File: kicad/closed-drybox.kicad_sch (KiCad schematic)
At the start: 30 parts, among them J1 Power_Jack, M1 Fan, M2 Fan, Q1 AO3400A, Q2 AO3400A, Q3 AO3400A, Q4 AO3400A, Q5 AO3400A, Q6 AO3400A, Q7 AO3400A, SW1 SW_PWR, U1 XIAO-ESP32-C6, U3 AMS1117-3.3

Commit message: add PCB
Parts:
- removed F1: Fuse, symbol Device:Fuse
- removed JP2, JP3: SolderJumper_2_Open, Jumper:SolderJumper-2_P1.3mm_Open_RoundedPad1.0x1.5mm, symbol Jumper:SolderJumper_2_Open
- removed SW1: SW_PWR, Connector_PinHeader_2.54mm:PinHeader_1x02_P2.54mm_Vertical, symbol CustomLibary:SW_PWR
- added H1, H2, H3, H4: MountingHole_Pad, MountingHole:MountingHole_3.2mm_M3_DIN965_Pad, symbol Mechanical:MountingHole_Pad
- C1: footprint (none) -> Capacitor_SMD:C_1206_3216Metric
- C6: renamed from C2; footprint (none) -> Capacitor_SMD:C_1206_3216Metric
- Q1: renamed from Q2; footprint Package_TO_SOT_SMD:SOT-23_Handsoldering -> Package_TO_SOT_SMD:SOT-23
- Q2: renamed from Q3; footprint Package_TO_SOT_SMD:SOT-23_Handsoldering -> Package_TO_SOT_SMD:SOT-23
- Q3: renamed from Q1; footprint Package_TO_SOT_SMD:SOT-23_Handsoldering -> Package_TO_SOT_SMD:SOT-23
- Q4, Q5, Q6, Q7: footprint Package_TO_SOT_SMD:SOT-23_Handsoldering -> Package_TO_SOT_SMD:SOT-23
- renumbered C4 to C2, C5 to C3, C6 to C4, C7 to C5, D3 to D1, D4 to D2, M2 to M1, M1 to M2, U3 to U1, U1 to U2
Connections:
- net GND: now also H1.1, H2.1, H3.1, H4.1
- net power measurement/IN: now also J1.1

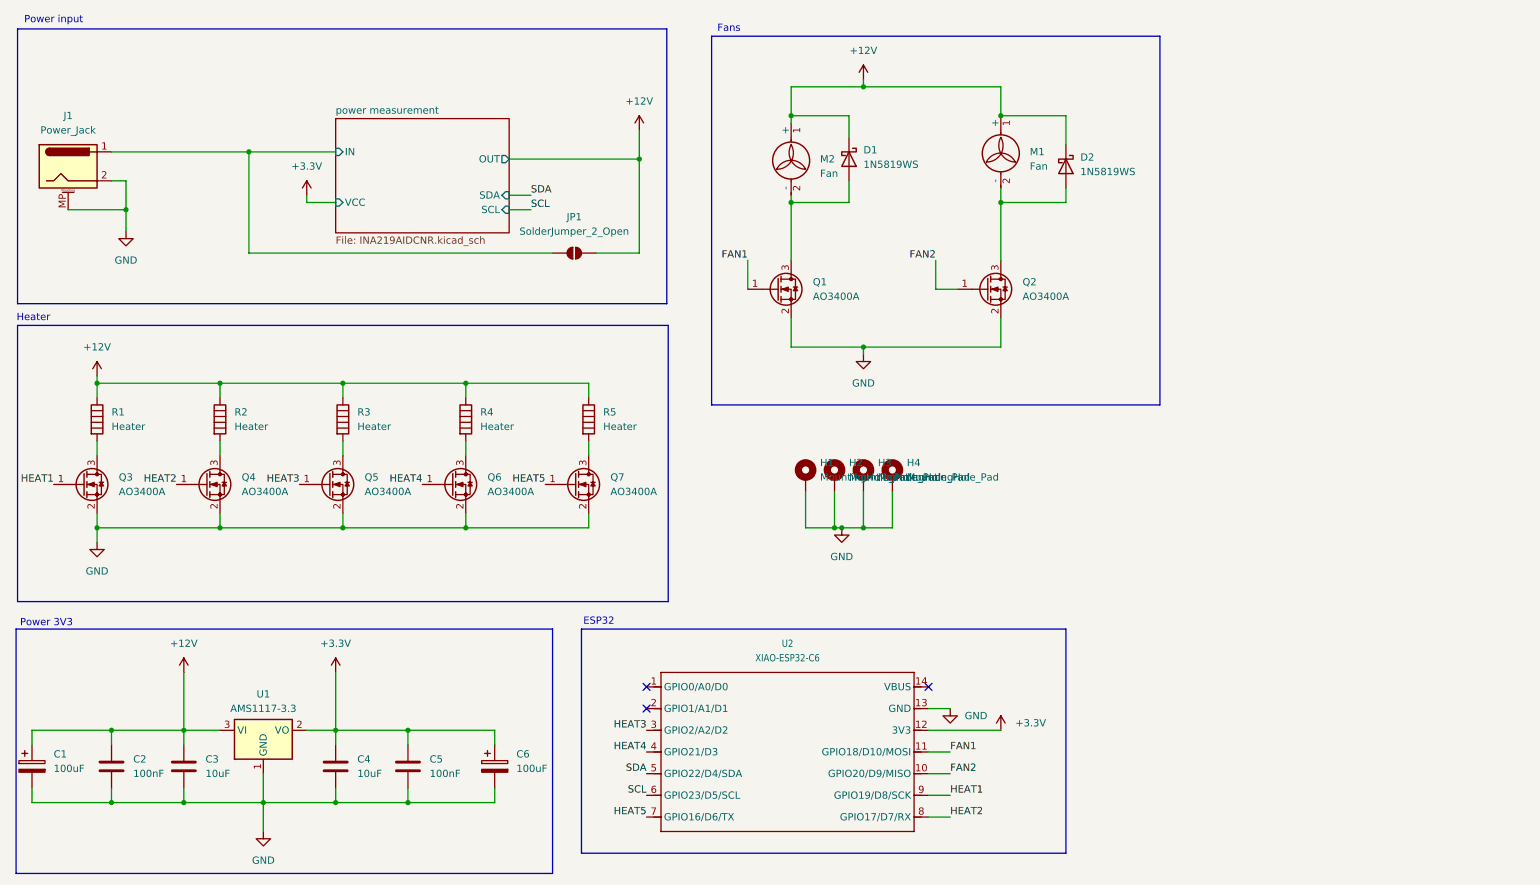
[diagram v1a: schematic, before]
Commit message: update schematic
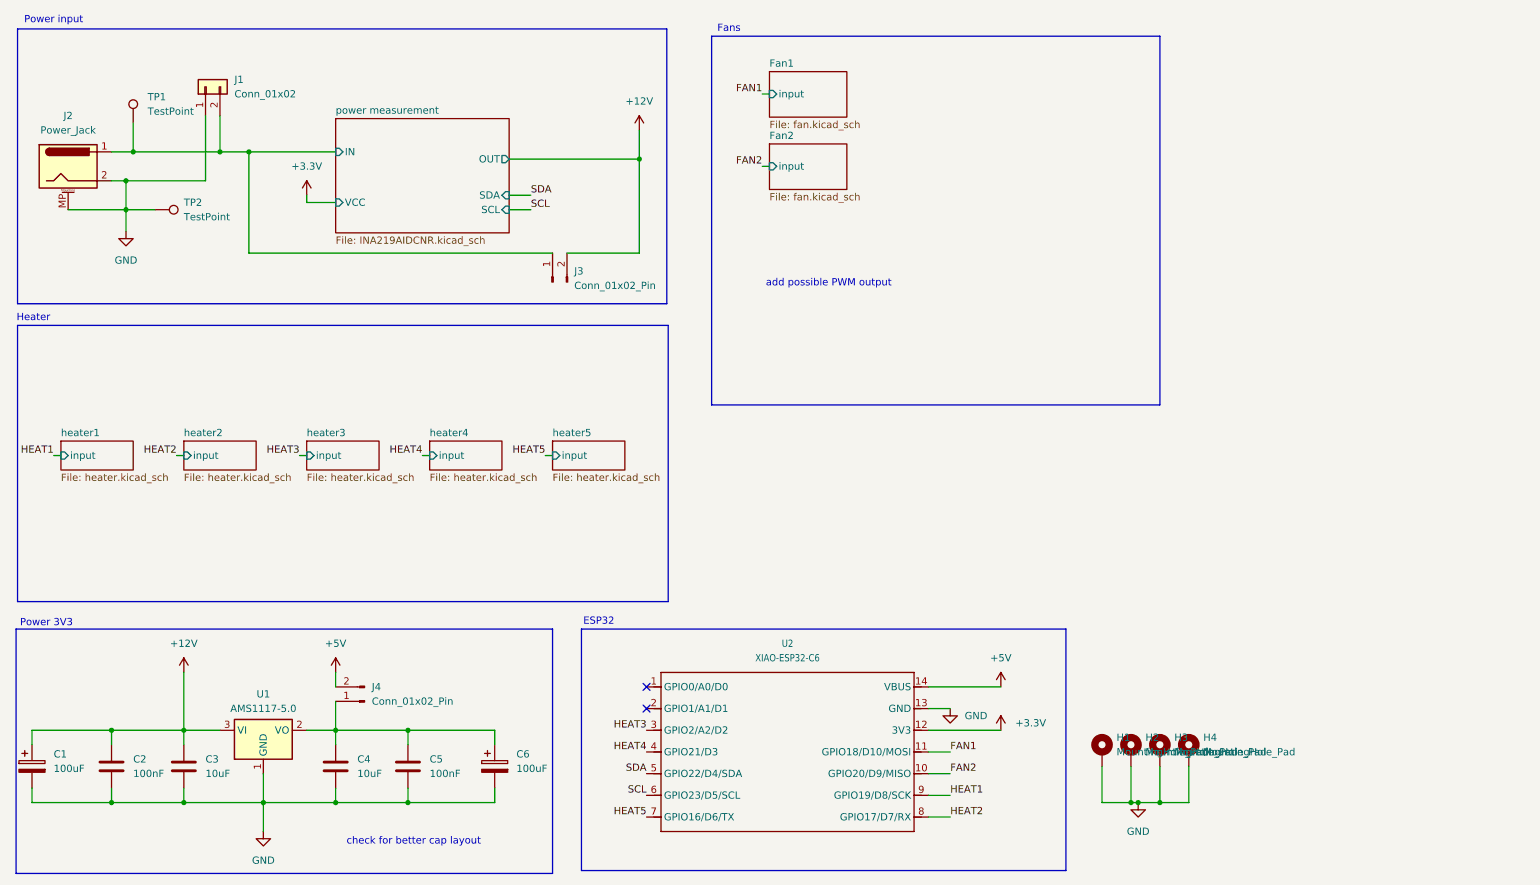
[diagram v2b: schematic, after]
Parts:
- removed D1, D2: 1N5819WS, Diode_SMD:D_SOD-323, symbol Diode:1N5819WS
- removed JP1: SolderJumper_2_Open, Jumper:SolderJumper-2_P1.3mm_Open_RoundedPad1.0x1.5mm, symbol Jumper:SolderJumper_2_Open
- removed M1, M2: Fan, Connector_JST:JST_XH_S2B-XH-A_1x02_P2.50mm_Horizontal, symbol Motor:Fan
- removed Q1, Q2, Q3, Q4, Q5, Q6, Q7: AO3400A, Package_TO_SOT_SMD:SOT-23, symbol Transistor_FET:AO3400A
- removed R1, R2, R3, R4, R5: Heater, Connector_JST:JST_XH_S2B-XH-A_1x02_P2.50mm_Horizontal, symbol Device:Heater
- removed U1: AMS1117-3.3, Package_TO_SOT_SMD:SOT-223-3_TabPin2, symbol Regulator_Linear:AMS1117-3.3
- added J1: Conn_01x02, Connector_JST:JST_XH_S2B-XH-A-1_1x02_P2.50mm_Horizontal, symbol Connector_Generic:Conn_01x02
- added J3, J4: Conn_01x02_Pin, Connector_PinHeader_2.54mm:PinHeader_1x02_P2.54mm_Vertical, symbol Connector:Conn_01x02_Pin
- added TP1, TP2: TestPoint, TestPoint:TestPoint_Pad_D2.5mm, symbol Connector:TestPoint
- added U1: AMS1117-5.0, Package_TO_SOT_SMD:SOT-223-3_TabPin2, symbol Regulator_Linear:AMS1117-5.0
- renumbered J1 to J2
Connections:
- net +12V: now also J3.2 (Pin_2), U1.3 (VI)
- net +3.3V: no longer C4.1, C5.1, C6.1
- net GND: now also J1.1 (Pin_1), TP2.1, U1.1 (GND)
- net power measurement/IN: now also J1.2 (Pin_2), J3.1 (Pin_1), TP1.1
- net +5V: now reaches U2.14 (VBUS)
- net +5V: now also J4.2 (Pin_2)
- new net: C4.1, C5.1, C6.1, J4.1 (Pin_1), U1.2 (VO)
- no-connect marks 3 -> 2
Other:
- added sheet Fan1 (fan.kicad_sch)
- added sheet Fan2 (fan.kicad_sch)
- added sheet heater1 (heater.kicad_sch)
- added sheet heater2 (heater.kicad_sch)
- added sheet heater3 (heater.kicad_sch)
- added sheet heater4 (heater.kicad_sch)
- added sheet heater5 (heater.kicad_sch)
- note added: "add possible PWM output"
- note added: "check for better cap layout"
- moved on the sheet: H1, H2, H3, H4

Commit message: added connectors
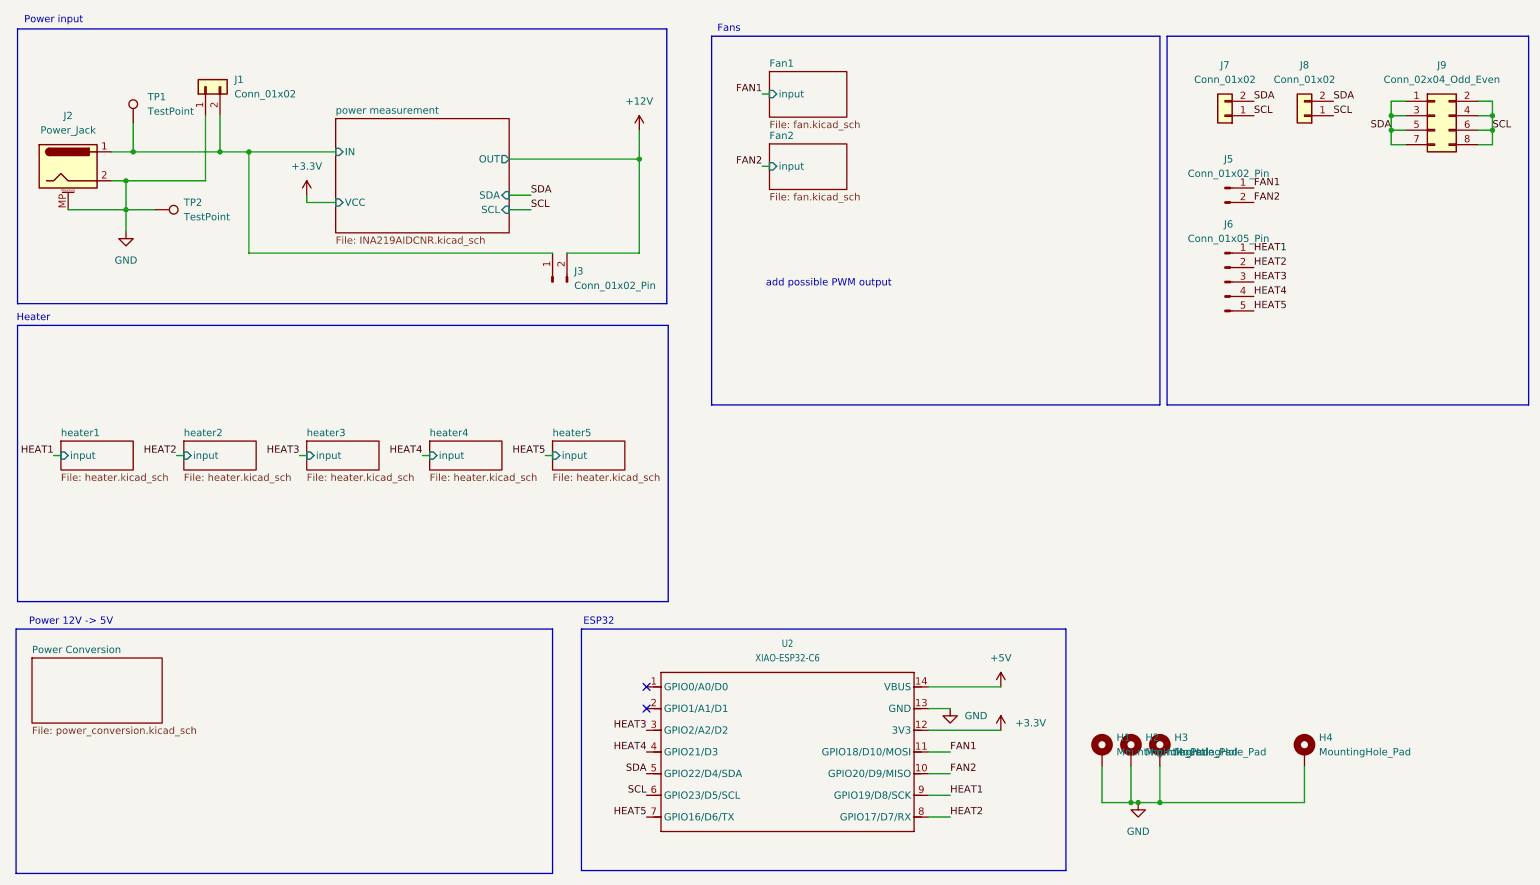
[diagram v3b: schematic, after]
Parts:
- removed C1, C6: 100uF, Capacitor_SMD:C_1206_3216Metric, symbol Device:C_Polarized
- removed C2, C5: 100nF, Capacitor_SMD:C_0603_1608Metric, symbol Device:C
- removed C3, C4: 10uF, Capacitor_SMD:C_0603_1608Metric, symbol Device:C
- removed J4: Conn_01x02_Pin, Connector_PinHeader_2.54mm:PinHeader_1x02_P2.54mm_Vertical, symbol Connector:Conn_01x02_Pin
- removed U1: AMS1117-5.0, Package_TO_SOT_SMD:SOT-223-3_TabPin2, symbol Regulator_Linear:AMS1117-5.0
- added J5: Conn_01x02_Pin, Connector_PinHeader_2.54mm:PinHeader_1x02_P2.54mm_Vertical, symbol Connector:Conn_01x02_Pin
- added J6: Conn_01x05_Pin, Connector_PinHeader_2.54mm:PinHeader_1x05_P2.54mm_Vertical, symbol Connector:Conn_01x05_Pin
- added J7, J8: Conn_01x02, Connector_JST:JST_XH_S2B-XH-A-1_1x02_P2.50mm_Horizontal, symbol Connector_Generic:Conn_01x02
- added J9: Conn_02x04_Odd_Even, symbol Connector_Generic:Conn_02x04_Odd_Even
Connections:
- net FAN1: now also J5.1 (Pin_1)
- net FAN2: now also J5.2 (Pin_2)
- net HEAT1: now also J6.1 (Pin_1)
- net HEAT2: now also J6.2 (Pin_2)
- net HEAT3: now also J6.3 (Pin_3)
- net HEAT4: now also J6.4 (Pin_4)
- net HEAT5: now also J6.5 (Pin_5)
- net SCL: now also J7.1 (Pin_1), J8.1 (Pin_1), J9.2 (Pin_2), J9.4 (Pin_4), J9.6 (Pin_6), J9.8 (Pin_8)
- net SDA: now also J7.2 (Pin_2), J8.2 (Pin_2), J9.1 (Pin_1), J9.3 (Pin_3), J9.5 (Pin_5), J9.7 (Pin_7)
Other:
- added sheet Power Conversion (power_conversion.kicad_sch)
- note added: "Power 12V -> 5V"
- note removed: "Power 3V3"
- note removed: "check for better cap layout"
- moved on the sheet: H4

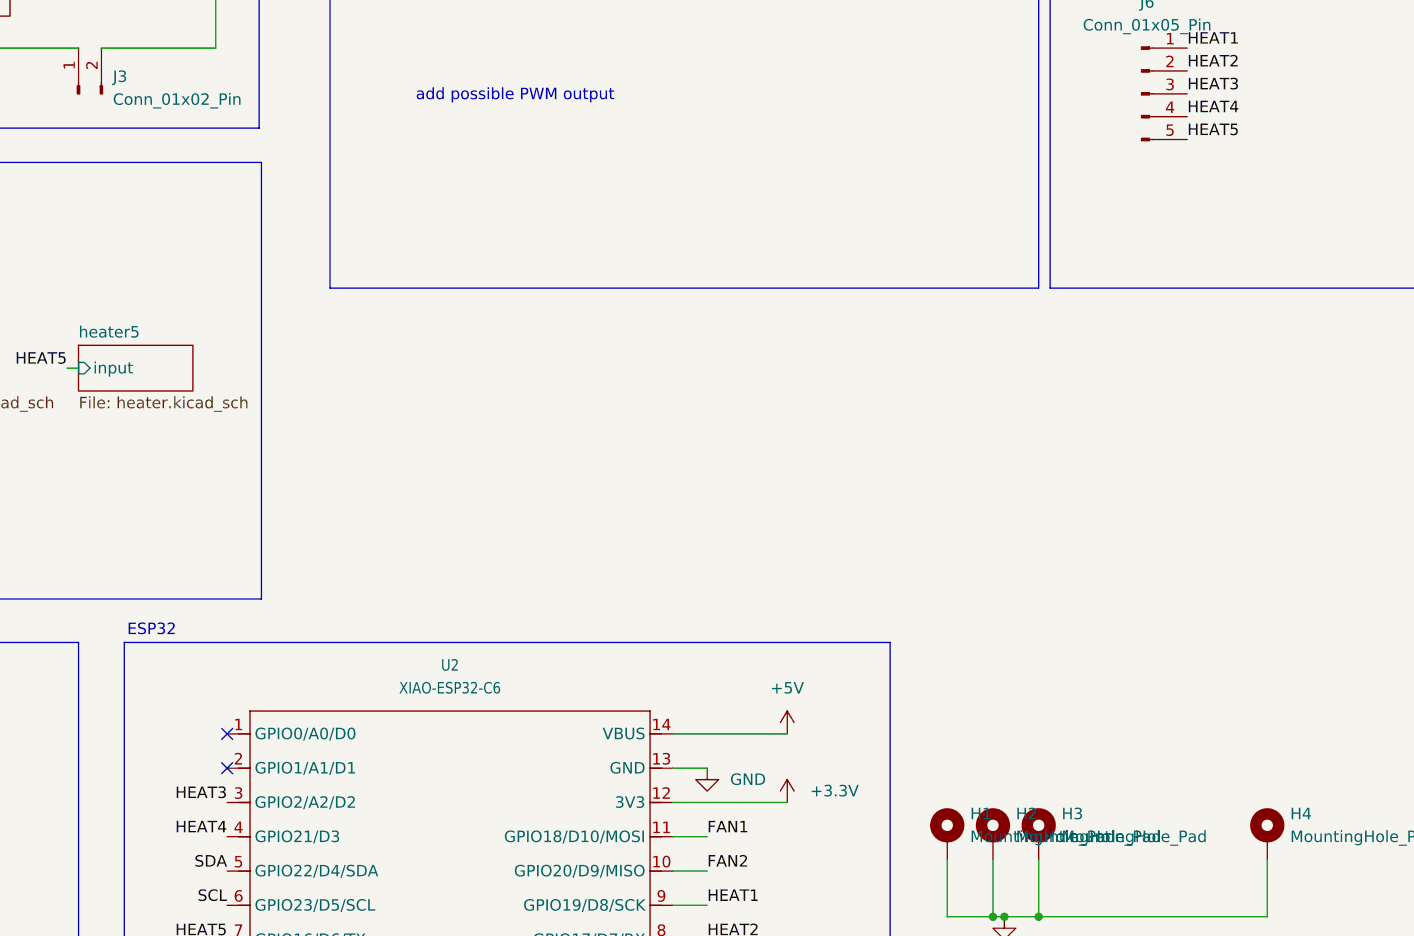
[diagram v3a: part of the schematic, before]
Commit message: added connectors to schematic
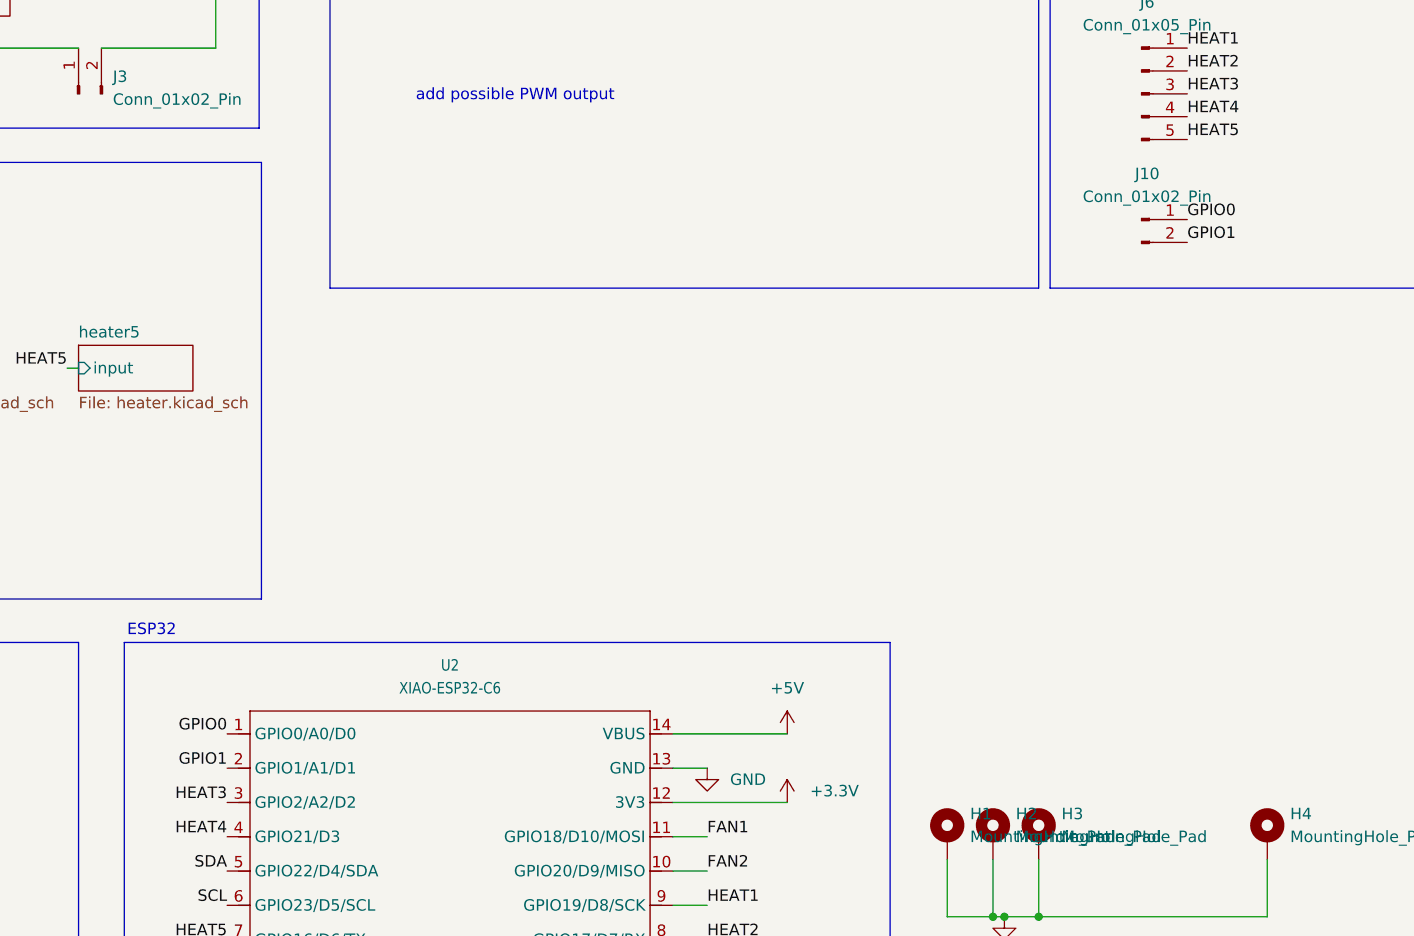
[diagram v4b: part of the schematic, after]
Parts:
- added J10: Conn_01x02_Pin, Connector_PinHeader_2.54mm:PinHeader_1x02_P2.54mm_Vertical, symbol Connector:Conn_01x02_Pin
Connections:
- net GPIO0: now reaches U2.1 (GPIO0/A0/D0)
- net GPIO0: now also J10.1 (Pin_1)
- net GPIO1: now reaches U2.2 (GPIO1/A1/D1)
- net GPIO1: now also J10.2 (Pin_2)
- no-connect marks 2 -> 0
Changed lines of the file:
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@@
 		(color 0 0 0 0)
-	)
-	(no_connect
-		(at 125.73 137.16)
-	)
-	(no_connect
-		(at 125.73 133.35)
 	)
 	(wire
@@
 		)
 	)
+	(label "GPIO0"
+		(at 232.41 76.2 0)
+		(effects
+			(font
+				(size 1.27 1.27)
+			)
+			(justify left bottom)
+		)
+	)
+	(label "GPIO0"
+		(at 125.73 133.35 180)
+		(effects
+			(font
+				(size 1.27 1.27)
+			)
+			(justify right bottom)
+		)
+	)
 	(label "HEAT3"
 		(at 232.41 62.23 0)
@@
 	(label "FAN2"
 		(at 146.05 41.91 180)
+		(effects
+			(font
+				(size 1.27 1.27)
+			)
+			(justify right bottom)
+		)
+	)
+	(label "GPIO1"
+		(at 232.41 78.74 0)
+		(effects
+			(font
+				(size 1.27 1.27)
+			)
+			(justify left bottom)
+		)
+	)
+	(label "GPIO1"
+		(at 125.73 137.16 180)
 		(effects
 			(font
@@
 					(unit 1)
 				)
+			)
+		)
+	)
+	(symbol
+		(lib_id "Connector:Conn_01x02_Pin")
+		(at 227.33 76.2 0)
+		(unit 1)
+		(exclude_from_sim no)
+		(in_bom yes)
+		(on_board yes)
+		(dnp no)
+		(fields_autoplaced yes)
+		(property "Reference" "J10"
+			(at 227.965 71.12 0)
+			(effects
+				(font
+					(size 1.27 1.27)
+				)
+			)
+		)
+		(property "Value" "Conn_01x02_Pin"
+			(at 227.965 73.66 0)
+			(effects
+				(font
+					(size 1.27 1.27)
+				)
+			)
+		)
+		(property "Footprint" "Connector_PinHeader_2.54mm:PinHeader_1x02_P2.54mm_Vertical"
+			(at 227.33 76.2 0)
+			(effects
+				(font
+					(size 1.27 1.27)
+				)
+				(hide yes)
+			)
+		)
+		(property "Datasheet" "~"
+			(at 227.33 76.2 0)
+			(effects
+				(font
+					(size 1.27 1.27)
+				)
+				(hide yes)
+			)
+		)
+		(property "Description" "Generic connector, single row, 01x02, script generated"
+			(at 227.33 76.2 0)
+			(effects
+				(font
+					(size 1.27 1.27)
+				)
+				(hide yes)
+			)
+		)
+		(pin "1"
+		)
+		(pin "2"
+		)
+		(instances
+			(project "closed-drybox"
+				(path "/99399f2a-756c-4718-9b6a-bb37855e6538"
+					(reference "J10")
+					(unit 1)
+				)
